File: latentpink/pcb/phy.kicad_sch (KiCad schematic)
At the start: 173 parts, among them J1 CONN_SFP_HOST, J18 BEL_FUSE_0845-2R1T-E4, J19 BEL_FUSE_0845-2R1T-E4, J2 SFP_CAGE, J20 BEL_FUSE_0845-2R1T-E4, J21 BEL_FUSE_0845-2R1T-E4, J3 XILINX_JTAG, J4 BEL_FUSE_0845-2R1T-E4, J8 BEL_FUSE_0845-2R1T-E4, M1 960-27-12-D-AB-0, U1 VSC8512, U2 XC7K160T-2FBG484C, U24 SIT9121AI-2BF-XXS200.000000G, U25 SIT9121AI-2BF-XXS156.250000G, U31 74LVC1T45, U32 74LVC1T45, U33 74LVC1T45, U34 74LVC1T45, U35 SIT9121AC-2B2-33E125.000000, U4 STM32H735-UFBGA176-25, U40 RCLAMP0514M, U41 RCLAMP0514M, U42 RCLAMP0514M, U43 RCLAMP0514M, U44 RCLAMP0514M, U45 RCLAMP0514M, U46 RCLAMP0514M, U47 RCLAMP0514M, U48 RCLAMP0514M, U49 RCLAMP0514M, U50 RCLAMP0514M, U51 RCLAMP0514M, U52 RCLAMP0514M, U53 RCLAMP0514M, U54 RCLAMP0514M, U55 RCLAMP0514M, U56 RCLAMP0514M, U57 RCLAMP0514M, U58 RCLAMP0514M, U59 RCLAMP0514M, U60 RCLAMP0514M, U61 RCLAMP0514M, U62 RCLAMP0514M, U63 RCLAMP0514M

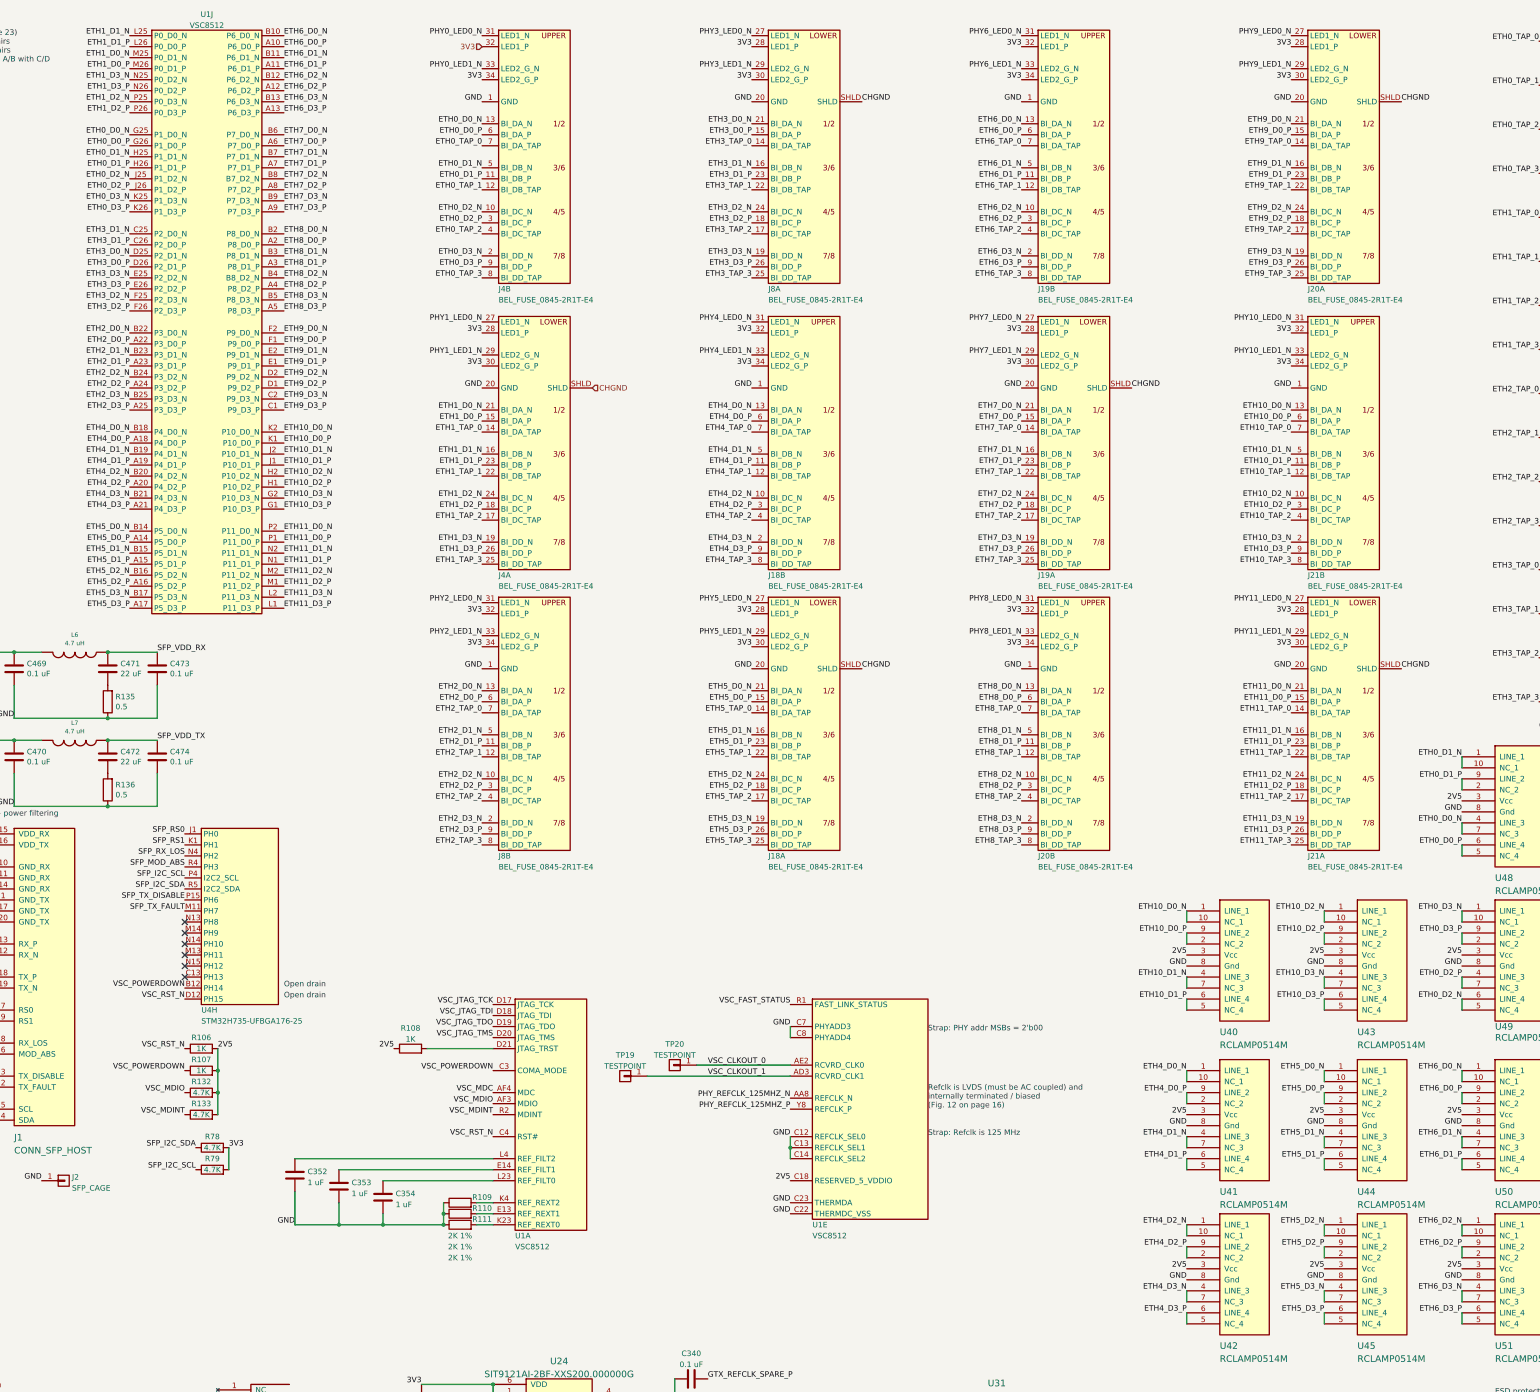
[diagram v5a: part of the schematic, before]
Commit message: Continued layout of VSC8512
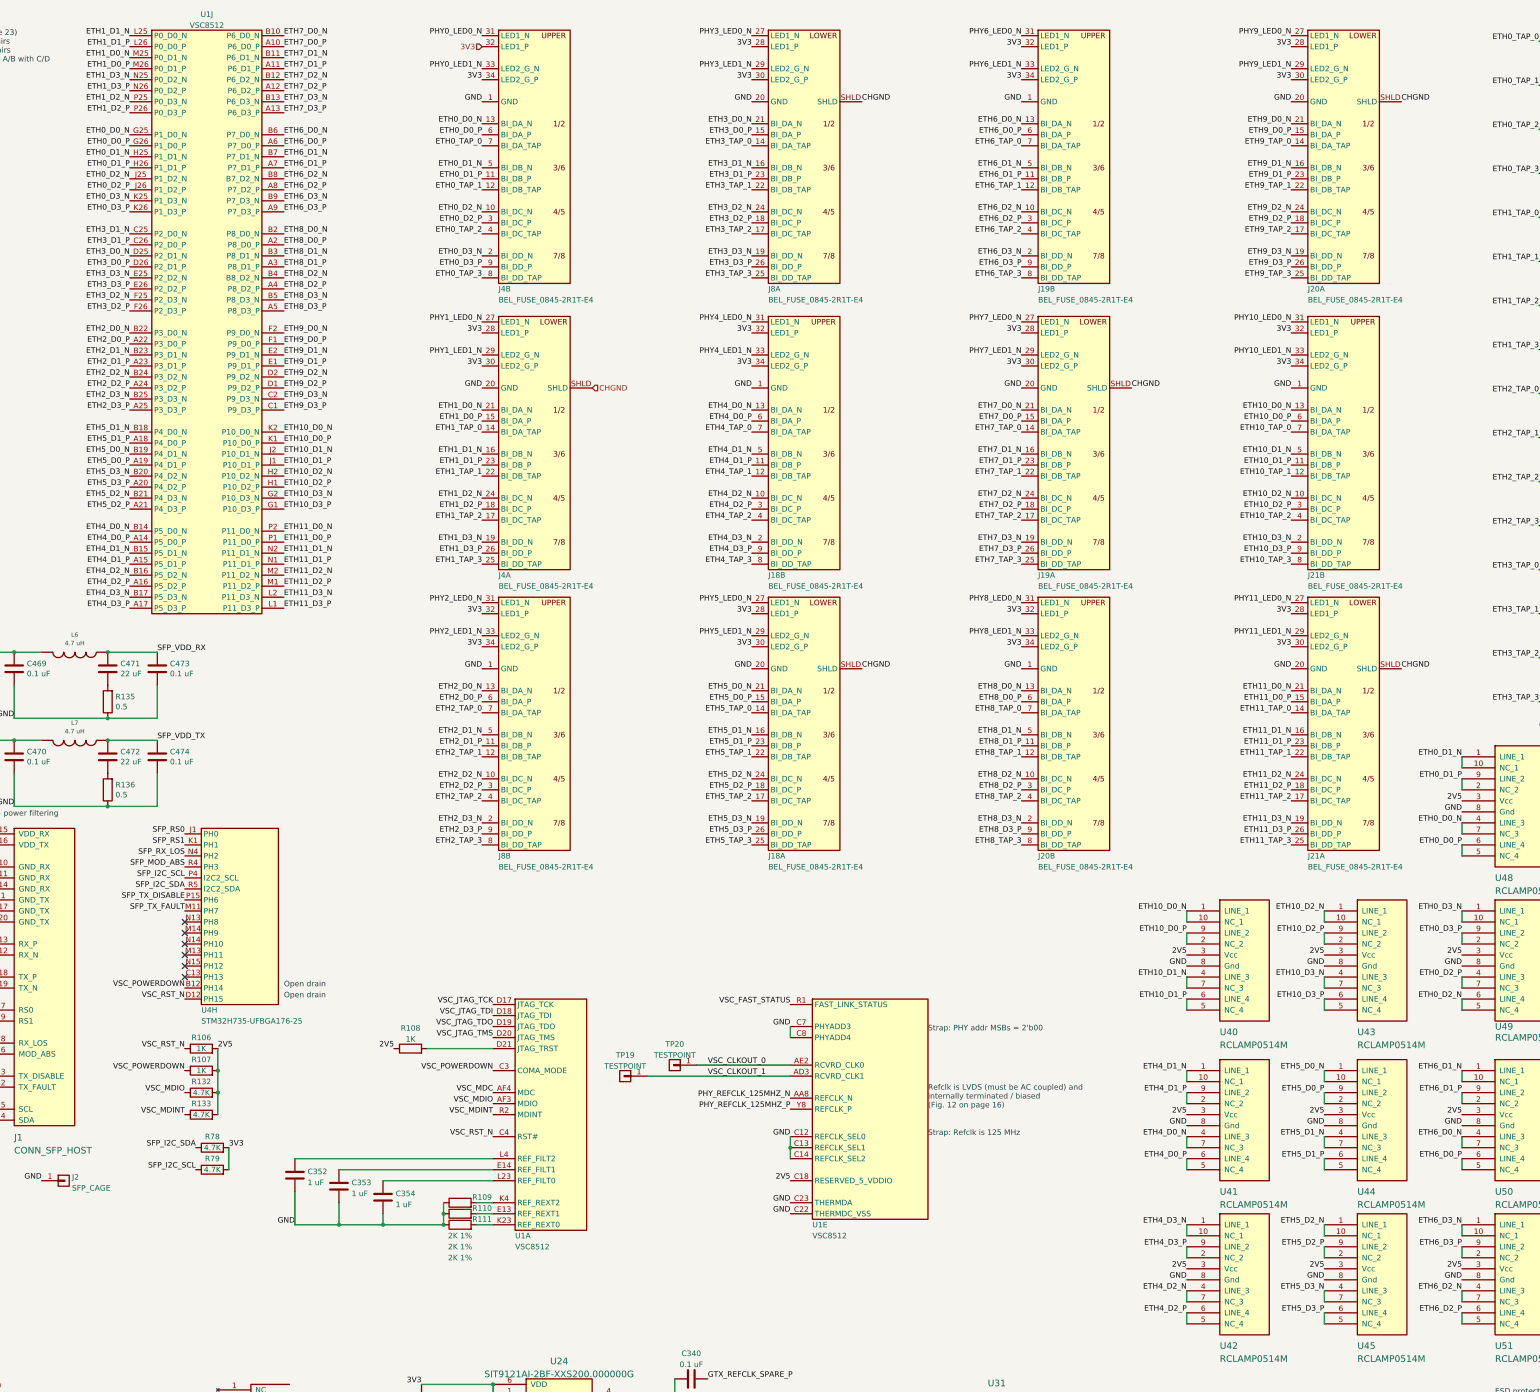
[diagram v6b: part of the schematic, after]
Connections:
- net ETH4_D0_N: now also U1.B14 (P5_D0_N), U41.4 (LINE_3), U41.7 (NC_3); no longer U1.B18 (P4_D0_N), U41.1 (LINE_1), U41.10 (NC_1)
- net ETH4_D0_P: now also U1.A14 (P5_D0_P), U41.5 (NC_4), U41.6 (LINE_4); no longer U1.A18 (P4_D0_P), U41.2 (NC_2), U41.9 (LINE_2)
- net ETH4_D1_N: now also U1.B15 (P5_D1_N), U41.1 (LINE_1), U41.10 (NC_1); no longer U1.B19 (P4_D1_N), U41.4 (LINE_3), U41.7 (NC_3)
- net ETH4_D1_P: now also U1.A15 (P5_D1_P), U41.2 (NC_2), U41.9 (LINE_2); no longer U1.A19 (P4_D1_P), U41.5 (NC_4), U41.6 (LINE_4)
- net ETH4_D2_N: now also U1.B16 (P5_D2_N), U42.4 (LINE_3), U42.7 (NC_3); no longer U1.B20 (P4_D2_N), U42.1 (LINE_1), U42.10 (NC_1)
- net ETH4_D2_P: now also U1.A16 (P5_D2_P), U42.5 (NC_4), U42.6 (LINE_4); no longer U1.A20 (P4_D2_P), U42.2 (NC_2), U42.9 (LINE_2)
- net ETH4_D3_N: now also U1.B17 (P5_D3_N), U42.1 (LINE_1), U42.10 (NC_1); no longer U1.B21 (P4_D3_N), U42.4 (LINE_3), U42.7 (NC_3)
- net ETH4_D3_P: now also U1.A17 (P5_D3_P), U42.2 (NC_2), U42.9 (LINE_2); no longer U1.A21 (P4_D3_P), U42.5 (NC_4), U42.6 (LINE_4)
- net ETH5_D0_N: now also U1.B19 (P4_D1_N); no longer U1.B14 (P5_D0_N)
- net ETH5_D0_P: now also U1.A19 (P4_D1_P); no longer U1.A14 (P5_D0_P)
- net ETH5_D1_N: now also U1.B18 (P4_D0_N); no longer U1.B15 (P5_D1_N)
- net ETH5_D1_P: now also U1.A18 (P4_D0_P); no longer U1.A15 (P5_D1_P)
- net ETH5_D2_N: now also U1.B21 (P4_D3_N); no longer U1.B16 (P5_D2_N)
- net ETH5_D2_P: now also U1.A21 (P4_D3_P); no longer U1.A16 (P5_D2_P)
- net ETH5_D3_N: now also U1.B20 (P4_D2_N); no longer U1.B17 (P5_D3_N)
- net ETH5_D3_P: now also U1.A20 (P4_D2_P); no longer U1.A17 (P5_D3_P)
- net ETH6_D0_N: now also U1.B6 (P7_D0_N), U50.4 (LINE_3), U50.7 (NC_3); no longer U1.B10 (P6_D0_N), U50.1 (LINE_1), U50.10 (NC_1)
- net ETH6_D0_P: now also U1.A6 (P7_D0_P), U50.5 (NC_4), U50.6 (LINE_4); no longer U1.A10 (P6_D0_P), U50.2 (NC_2), U50.9 (LINE_2)
- net ETH6_D1_N: now also U1.B7 (P7_D1_N), U50.1 (LINE_1), U50.10 (NC_1); no longer U1.B11 (P6_D1_N), U50.4 (LINE_3), U50.7 (NC_3)
- net ETH6_D1_P: now also U1.A7 (P7_D1_P), U50.2 (NC_2), U50.9 (LINE_2); no longer U1.A11 (P6_D1_P), U50.5 (NC_4), U50.6 (LINE_4)
- net ETH6_D2_N: now also U1.B8 (B7_D2_N), U51.4 (LINE_3), U51.7 (NC_3); no longer U1.B12 (P6_D2_N), U51.1 (LINE_1), U51.10 (NC_1)
- net ETH6_D2_P: now also U1.A8 (P7_D2_P), U51.5 (NC_4), U51.6 (LINE_4); no longer U1.A12 (P6_D2_P), U51.2 (NC_2), U51.9 (LINE_2)
- net ETH6_D3_N: now also U1.B9 (P7_D3_N), U51.1 (LINE_1), U51.10 (NC_1); no longer U1.B13 (P6_D3_N), U51.4 (LINE_3), U51.7 (NC_3)
- net ETH6_D3_P: now also U1.A9 (P7_D3_P), U51.2 (NC_2), U51.9 (LINE_2); no longer U1.A13 (P6_D3_P), U51.5 (NC_4), U51.6 (LINE_4)
- net ETH7_D0_N: now also U1.B10 (P6_D0_N); no longer U1.B6 (P7_D0_N)
- net ETH7_D0_P: now also U1.A10 (P6_D0_P); no longer U1.A6 (P7_D0_P)
- net ETH7_D1_N: now also U1.B11 (P6_D1_N); no longer U1.B7 (P7_D1_N)
- net ETH7_D1_P: now also U1.A11 (P6_D1_P); no longer U1.A7 (P7_D1_P)
- net ETH7_D2_N: now also U1.B12 (P6_D2_N); no longer U1.B8 (B7_D2_N)
- net ETH7_D2_P: now also U1.A12 (P6_D2_P); no longer U1.A8 (P7_D2_P)
- net ETH7_D3_N: now also U1.B13 (P6_D3_N); no longer U1.B9 (P7_D3_N)
- net ETH7_D3_P: now also U1.A13 (P6_D3_P); no longer U1.A9 (P7_D3_P)

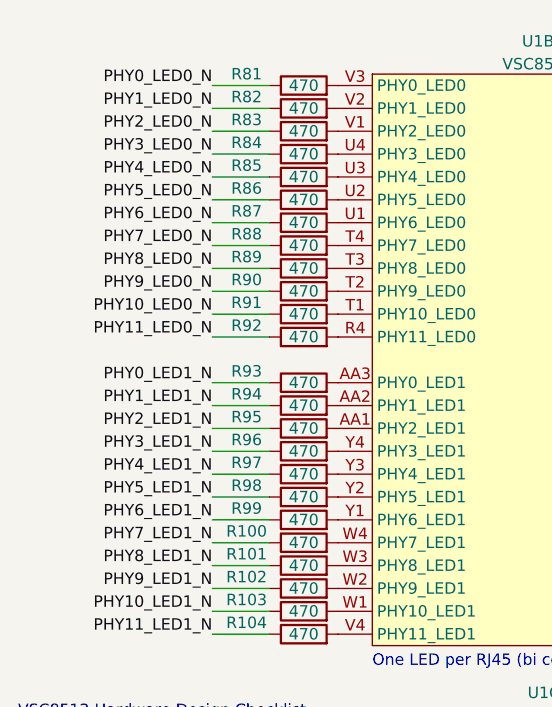
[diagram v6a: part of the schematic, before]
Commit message: Continued initial layout. Working on PHY decoupling caps and fanout
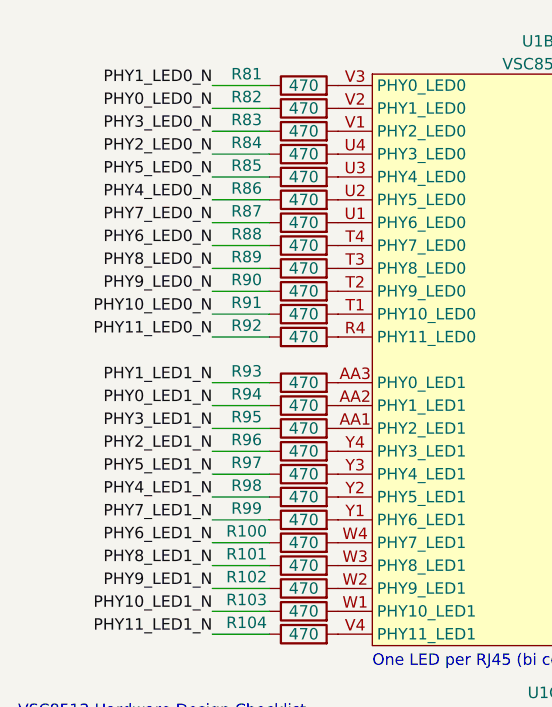
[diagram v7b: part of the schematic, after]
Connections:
- net PHY0_LED0_N: now also R82.1; no longer R81.1
- net PHY0_LED1_N: now also R94.1; no longer R93.1
- net PHY1_LED0_N: now also R81.1; no longer R82.1
- net PHY1_LED1_N: now also R93.1; no longer R94.1
- net PHY2_LED0_N: now also R84.1; no longer R83.1
- net PHY2_LED1_N: now also R96.1; no longer R95.1
- net PHY3_LED0_N: now also R83.1; no longer R84.1
- net PHY3_LED1_N: now also R95.1; no longer R96.1
- net PHY4_LED0_N: now also R86.1; no longer R85.1
- net PHY4_LED1_N: now also R98.1; no longer R97.1
- net PHY5_LED0_N: now also R85.1; no longer R86.1
- net PHY5_LED1_N: now also R97.1; no longer R98.1
- net PHY6_LED0_N: now also R88.1; no longer R87.1
- net PHY6_LED1_N: now also R100.1; no longer R99.1
- net PHY7_LED0_N: now also R87.1; no longer R88.1
- net PHY7_LED1_N: now also R99.1; no longer R100.1
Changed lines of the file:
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@@
     (effects (font (size 1.27 1.27)) (justify right bottom))
   )
-  (label "PHY4_LED0_N" (at 38.1 31.75 180)
+  (label "PHY4_LED0_N" (at 38.1 34.29 180)
     (effects (font (size 1.27 1.27)) (justify right bottom))
   )
@@
     (effects (font (size 1.27 1.27)) (justify right bottom))
   )
-  (label "PHY7_LED0_N" (at 38.1 39.37 180)
+  (label "PHY7_LED0_N" (at 38.1 36.83 180)
     (effects (font (size 1.27 1.27)) (justify right bottom))
   )
@@
     (effects (font (size 1.27 1.27)) (justify right bottom))
   )
-  (label "PHY1_LED1_N" (at 38.1 57.15 180)
+  (label "PHY1_LED1_N" (at 38.1 54.61 180)
     (effects (font (size 1.27 1.27)) (justify right bottom))
   )
@@
     (effects (font (size 1.27 1.27)) (justify right bottom))
   )
-  (label "PHY4_LED1_N" (at 38.1 64.77 180)
+  (label "PHY4_LED1_N" (at 38.1 67.31 180)
     (effects (font (size 1.27 1.27)) (justify right bottom))
   )
@@
     (effects (font (size 1.27 1.27)) (justify right bottom))
   )
-  (label "PHY0_LED1_N" (at 38.1 54.61 180)
+  (label "PHY0_LED1_N" (at 38.1 57.15 180)
     (effects (font (size 1.27 1.27)) (justify right bottom))
   )
@@
     (effects (font (size 1.27 1.27)) (justify right bottom))
   )
-  (label "PHY3_LED1_N" (at 38.1 62.23 180)
+  (label "PHY3_LED1_N" (at 38.1 59.69 180)
     (effects (font (size 1.27 1.27)) (justify right bottom))
   )
@@
     (effects (font (size 1.27 1.27)) (justify right bottom))
   )
-  (label "PHY2_LED0_N" (at 38.1 26.67 180)
+  (label "PHY2_LED0_N" (at 38.1 29.21 180)
     (effects (font (size 1.27 1.27)) (justify right bottom))
   )
@@
     (effects (font (size 1.27 1.27)) (justify left bottom))
   )
-  (label "PHY2_LED1_N" (at 38.1 59.69 180)
+  (label "PHY2_LED1_N" (at 38.1 62.23 180)
     (effects (font (size 1.27 1.27)) (justify right bottom))
   )
@@
     (effects (font (size 1.27 1.27)) (justify right bottom))
   )
-  (label "PHY1_LED0_N" (at 38.1 24.13 180)
+  (label "PHY1_LED0_N" (at 38.1 21.59 180)
     (effects (font (size 1.27 1.27)) (justify right bottom))
   )
@@
     (effects (font (size 1.27 1.27)) (justify right bottom))
   )
-  (label "PHY7_LED1_N" (at 38.1 72.39 180)
+  (label "PHY7_LED1_N" (at 38.1 69.85 180)
     (effects (font (size 1.27 1.27)) (justify right bottom))
   )
@@
     (effects (font (size 1.27 1.27)) (justify right bottom))
   )
-  (label "PHY5_LED1_N" (at 38.1 67.31 180)
+  (label "PHY5_LED1_N" (at 38.1 64.77 180)
     (effects (font (size 1.27 1.27)) (justify right bottom))
   )
@@
     (effects (font (size 1.27 1.27)) (justify right bottom))
   )
-  (label "PHY5_LED0_N" (at 38.1 34.29 180)
+  (label "PHY5_LED0_N" (at 38.1 31.75 180)
     (effects (font (size 1.27 1.27)) (justify right bottom))
   )
@@
     (effects (font (size 1.27 1.27)) (justify right bottom))
   )
-  (label "PHY6_LED1_N" (at 38.1 69.85 180)
+  (label "PHY6_LED1_N" (at 38.1 72.39 180)
     (effects (font (size 1.27 1.27)) (justify right bottom))
   )
@@
     (effects (font (size 1.27 1.27)) (justify right bottom))
   )
-  (label "PHY6_LED0_N" (at 38.1 36.83 180)
+  (label "PHY6_LED0_N" (at 38.1 39.37 180)
     (effects (font (size 1.27 1.27)) (justify right bottom))
   )
@@
     (effects (font (size 1.27 1.27)) (justify right bottom))
   )
-  (label "PHY3_LED0_N" (at 38.1 29.21 180)
+  (label "PHY3_LED0_N" (at 38.1 26.67 180)
     (effects (font (size 1.27 1.27)) (justify right bottom))
   )
@@
     (effects (font (size 1.27 1.27)) (justify left bottom))
   )
-  (label "PHY0_LED0_N" (at 38.1 21.59 180)
-    (effects (font (size 1.27 1.27)) (justify right bottom))
-  )
+  (label "PHY0_LED0_N" (at 38.1 24.13 180)
+    (effects (font (size 1.27 1.27)) (justify right bottom))
+  )
